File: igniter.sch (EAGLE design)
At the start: 19 parts, among them X1 RASPI_BOARD_B+#_H, X3 5566-4-RIGHTANGLE

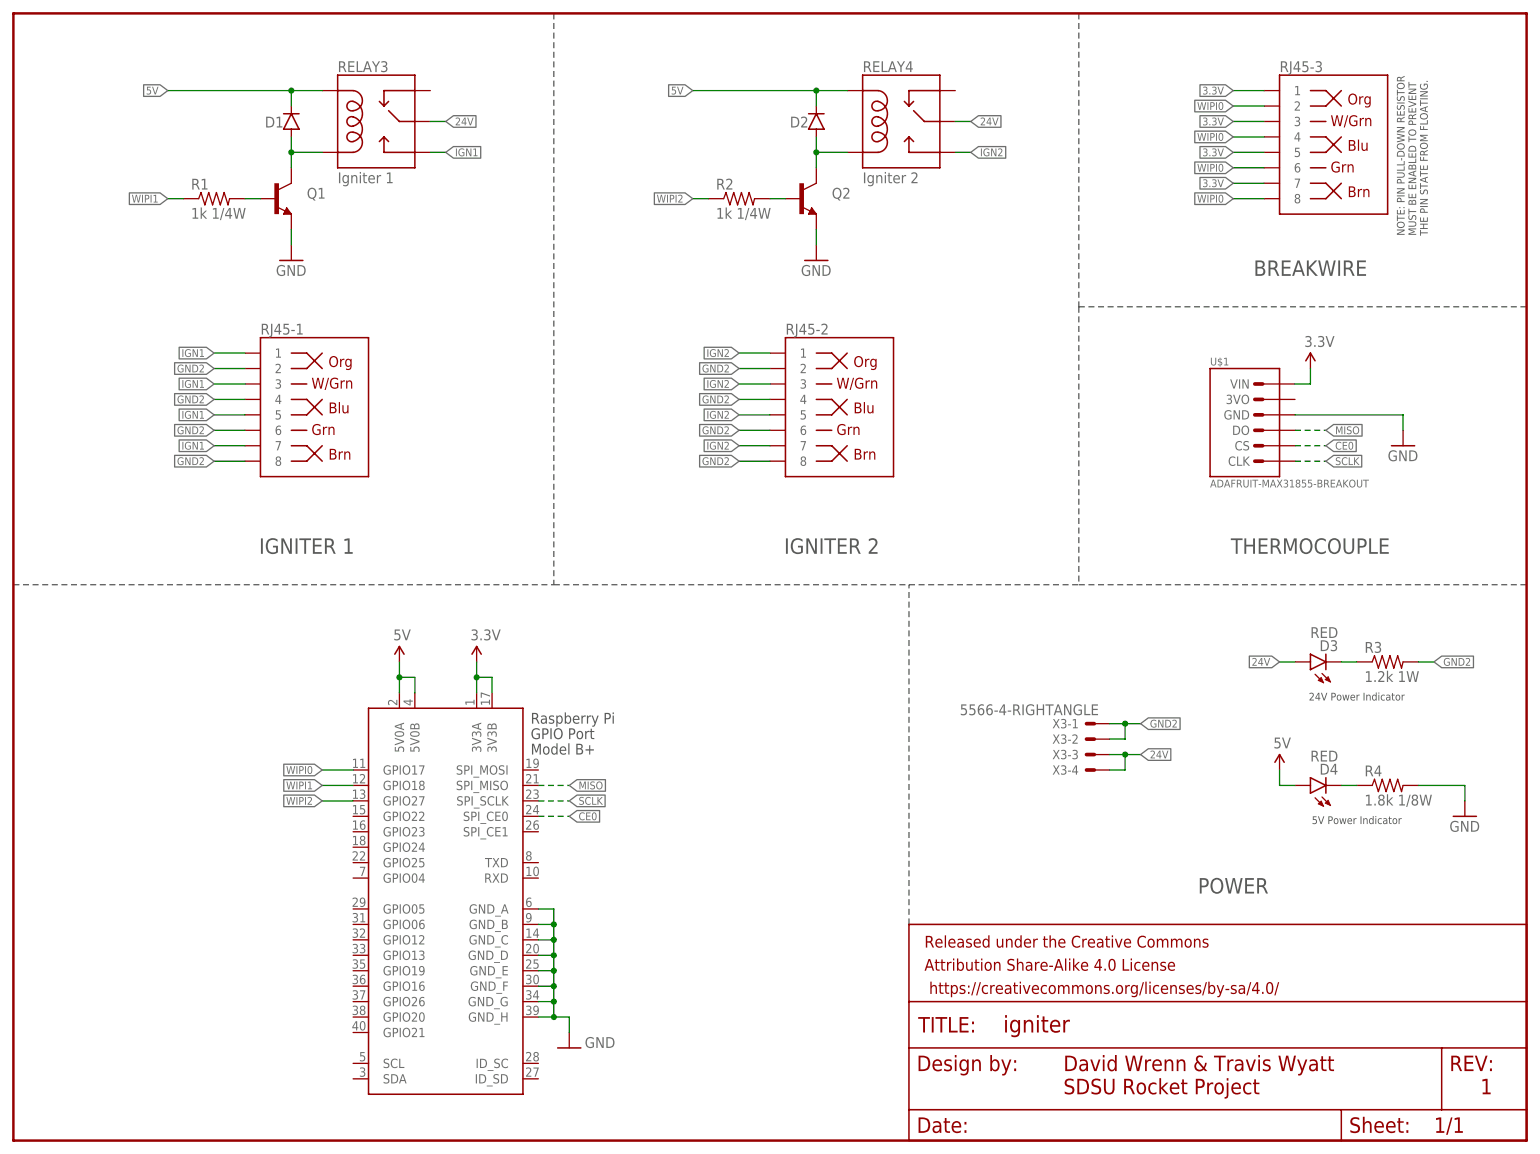
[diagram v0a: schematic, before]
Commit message: Power connector and resistor updates. Added PCB images (generated by OSHPark). Added README.md.
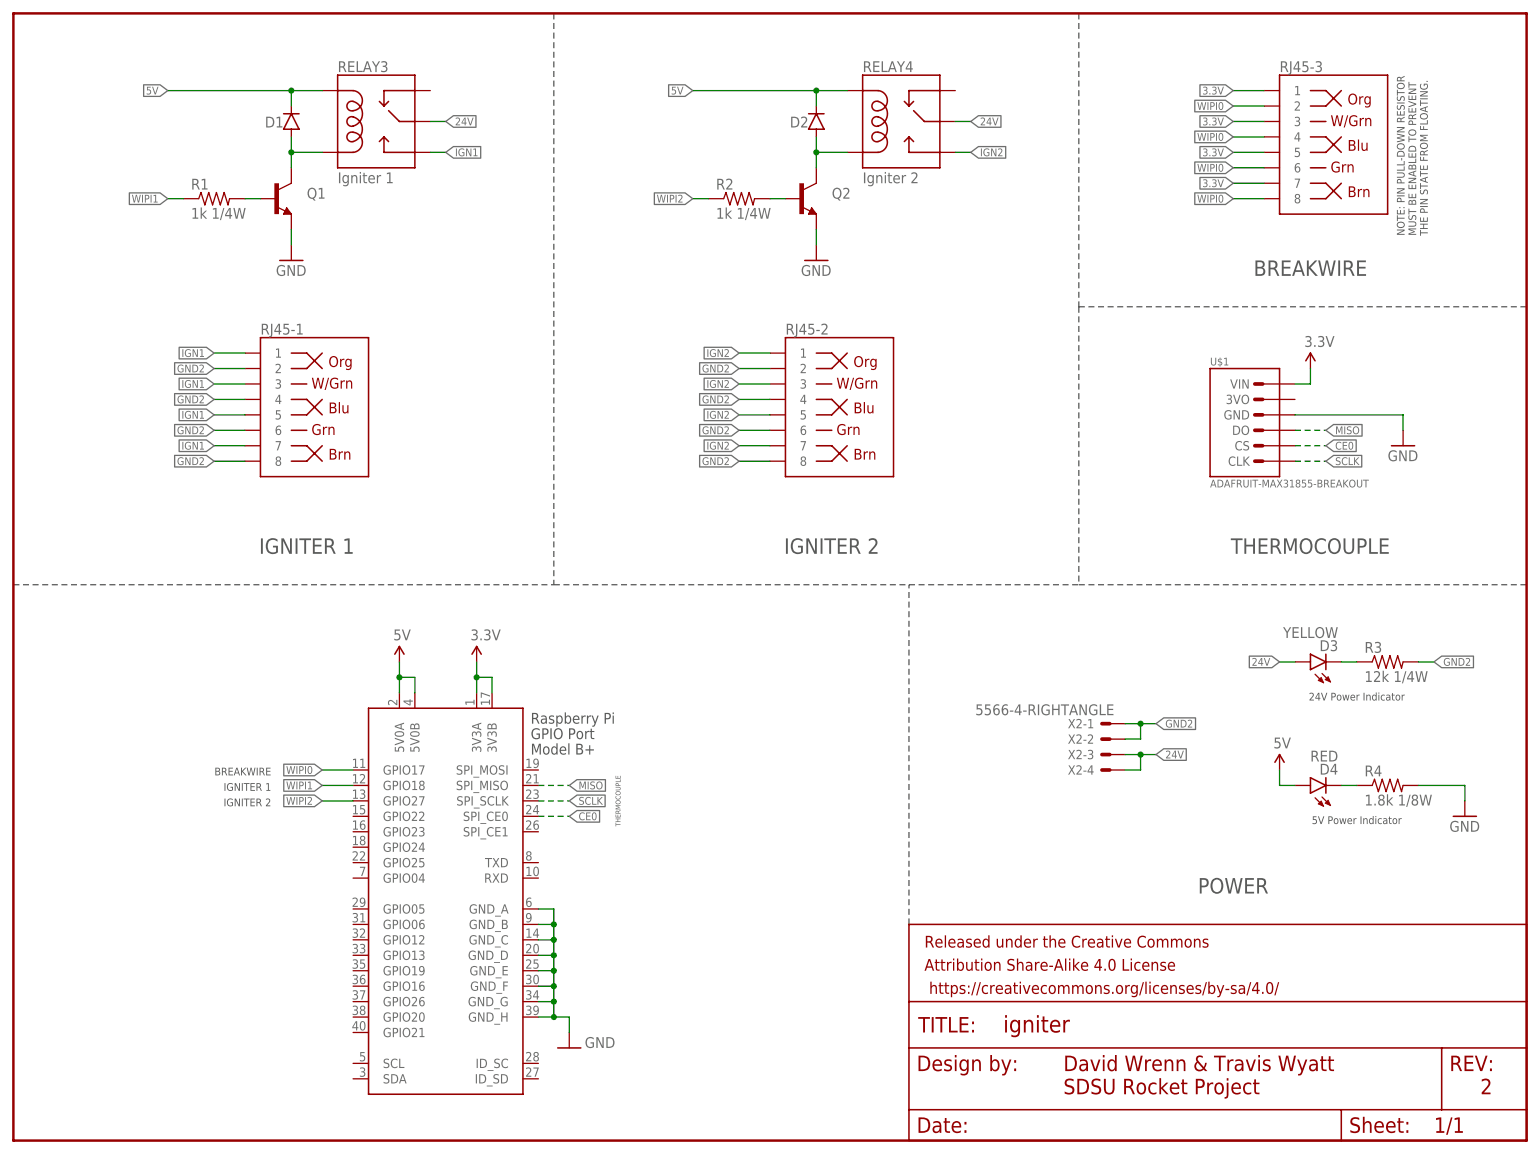
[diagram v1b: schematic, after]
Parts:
- removed X3: 5566-4-RIGHTANGLE, SDSURocket-BreakoutBoards:5566-4-RIGHTANGLE
- added X2: 5566-4-RIGHTANGLE, SDSURocket-Connectors:5566-4-RIGHTANGLE
- D3: value RED -> YELLOW
- R3: value 1.2k 1W -> 12k 1/4W; device SparkFun-Resistors:RESISTOR2512 -> SparkFun-Resistors:RESISTOR0603-RES
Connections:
- net 24V: now also X2-3.S, X2-4.S; no longer X3-3.S, X3-4.S
- net GND2: now also X2-1.S, X2-2.S; no longer X3-1.S, X3-2.S
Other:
- note added: "2"
- note removed: "1"
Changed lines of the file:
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@@
 <part name="RJ45-3" library="SparkFun-Connectors" deviceset="RJ45-8" device="PTH" value=""/>
 <part name="U$1" library="SDSURocket-BreakoutBoards" deviceset="ADAFRUIT-MAX31855" device="-BREAKOUT"/>
-<part name="X3" library="SDSURocket-BreakoutBoards" deviceset="5566-4" device="-RIGHTANGLE"/>
-<part name="D3" library="SparkFun-LED" deviceset="LED" device="0603" value="RED"/>
+<part name="D3" library="SparkFun-LED" deviceset="LED" device="0603" value="YELLOW"/>
 <part name="D4" library="SparkFun-LED" deviceset="LED" device="0603" value="RED"/>
-<part name="R3" library="SparkFun-Resistors" deviceset="RESISTOR" device="2512" value="1.2k 1W"/>
+<part name="R3" library="SparkFun-Resistors" deviceset="RESISTOR" device="0603-RES" value="12k 1/4W"/>
 <part name="R4" library="SparkFun-Resistors" deviceset="RESISTOR" device="0603-RES" value="1.8k 1/8W"/>
 <part name="GND2" library="SparkFun-Aesthetics" deviceset="GND" device=""/>
@@
 <part name="SUPPLY3" library="SparkFun-Aesthetics" deviceset="3.3V" device=""/>
 <part name="SUPPLY4" library="SparkFun-Aesthetics" deviceset="5V" device=""/>
+<part name="X2" library="SDSURocket-Connectors" deviceset="5566-4" device="-RIGHTANGLE"/>
 </parts>
 <sheets>
@@
 MUST BE ENABLED TO PREVENT
 THE PIN STATE FROM FLOATING.</text>
-<text x="241.3" y="7.62" size="2.54" layer="94">1</text>
+<text x="241.3" y="7.62" size="2.54" layer="94">2</text>
 <text x="172.72" y="12.7" size="2.54" layer="94" align="center-left">David Wrenn &amp; Travis Wyatt</text>
 <text x="172.72" y="8.89" size="2.54" layer="94" align="center-left">SDSU Rocket Project</text>
 <text x="220.98" y="73.66" size="1.27" layer="97" align="top-center">24V Power Indicator</text>
 <text x="220.98" y="53.34" size="1.27" layer="97" align="top-center">5V Power Indicator</text>
+<text x="42.418" y="60.706" size="1.27" layer="97" align="center-right">BREAKWIRE</text>
+<text x="42.418" y="58.166" size="1.27" layer="97" align="center-right">IGNITER 1</text>
+<text x="42.418" y="55.626" size="1.27" layer="97" align="center-right">IGNITER 2</text>
+<text x="99.06" y="55.88" size="0.8128" layer="97" rot="R90" align="top-center">THERMOCOUPLE</text>
 </plain>
 <instances>
@@
 <instance part="RJ45-3" gate="JP1" x="213.36" y="165.1"/>
 <instance part="U$1" gate="G$1" x="203.2" y="119.38"/>
-<instance part="X3" gate="-1" x="177.8" y="68.58" rot="MR0"/>
-<instance part="X3" gate="-2" x="177.8" y="66.04" rot="MR0"/>
-<instance part="X3" gate="-3" x="177.8" y="63.5" rot="MR0"/>
-<instance part="X3" gate="-4" x="177.8" y="60.96" rot="MR0"/>
 <instance part="D3" gate="G$1" x="213.36" y="78.74" rot="R90"/>
 <instance part="D4" gate="G$1" x="213.36" y="58.42" rot="R90"/>
@@
 <instance part="SUPPLY3" gate="G$1" x="213.36" y="127"/>
 <instance part="SUPPLY4" gate="G$1" x="208.28" y="60.96"/>
+<instance part="X2" gate="-1" x="180.34" y="68.58" rot="MR0"/>
+<instance part="X2" gate="-2" x="180.34" y="66.04" rot="MR0"/>
+<instance part="X2" gate="-3" x="180.34" y="63.5" rot="MR0"/>
+<instance part="X2" gate="-4" x="180.34" y="60.96" rot="MR0"/>
 </instances>
 <busses>
@@
 </segment>
 <segment>
-<pinref part="X3" gate="-3" pin="S"/>
-<wire x1="180.34" y1="63.5" x2="182.88" y2="63.5" width="0.1524" layer="91"/>
-<pinref part="X3" gate="-4" pin="S"/>
-<wire x1="182.88" y1="63.5" x2="185.42" y2="63.5" width="0.1524" layer="91"/>
-<wire x1="180.34" y1="60.96" x2="182.88" y2="60.96" width="0.1524" layer="91"/>
-<wire x1="182.88" y1="60.96" x2="182.88" y2="63.5" width="0.1524" layer="91"/>
-<junction x="182.88" y="63.5"/>
-<label x="185.42" y="63.5" size="1.27" layer="95" xref="yes"/>
-</segment>
-<segment>
 <pinref part="D3" gate="G$1" pin="A"/>
 <wire x1="210.82" y1="78.74" x2="208.28" y2="78.74" width="0.1524" layer="91"/>
 <label x="208.28" y="78.74" size="1.27" layer="95" rot="MR0" xref="yes"/>
+</segment>
+<segment>
+<pinref part="X2" gate="-3" pin="S"/>
+<wire x1="182.88" y1="63.5" x2="185.42" y2="63.5" width="0.1524" layer="91"/>
+<pinref part="X2" gate="-4" pin="S"/>
+<wire x1="185.42" y1="63.5" x2="187.96" y2="63.5" width="0.1524" layer="91"/>
+<wire x1="182.88" y1="60.96" x2="185.42" y2="60.96" width="0.1524" layer="91"/>
+<wire x1="185.42" y1="60.96" x2="185.42" y2="63.5" width="0.1524" layer="91"/>
+<junction x="185.42" y="63.5"/>
+<label x="187.96" y="63.5" size="1.27" layer="95" xref="yes"/>
 </segment>
 </net>
@@
 </segment>
 <segment>
-<pinref part="X3" gate="-1" pin="S"/>
-<wire x1="180.34" y1="68.58" x2="182.88" y2="68.58" width="0.1524" layer="91"/>
-<pinref part="X3" gate="-2" pin="S"/>
-<wire x1="182.88" y1="68.58" x2="185.42" y2="68.58" width="0.1524" layer="91"/>
-<wire x1="180.34" y1="66.04" x2="182.88" y2="66.04" width="0.1524" layer="91"/>
-<wire x1="182.88" y1="66.04" x2="182.88" y2="68.58" width="0.1524" layer="91"/>
-<junction x="182.88" y="68.58"/>
-<label x="185.42" y="68.58" size="1.27" layer="95" xref="yes"/>
-</segment>
-<segment>
 <pinref part="R3" gate="G$1" pin="2"/>
 <wire x1="231.14" y1="78.74" x2="233.68" y2="78.74" width="0.1524" layer="91"/>
 <label x="233.68" y="78.74" size="1.27" layer="95" xref="yes"/>
 </segment>
-</net>
+<segment>
+<pinref part="X2" gate="-1" pin="S"/>
+<wire x1="182.88" y1="68.58" x2="185.42" y2="68.58" width="0.1524" layer="91"/>
+<pinref part="X2" gate="-2" pin="S"/>
+<wire x1="185.42" y1="68.58" x2="187.96" y2="68.58" width="0.1524" layer="91"/>
+<wire x1="182.88" y1="66.04" x2="185.42" y2="66.04" width="0.1524" layer="91"/>
+<wire x1="185.42" y1="66.04" x2="185.42" y2="68.58" width="0.1524" layer="91"/>
+<junction x="185.42" y="68.58"/>
+<label x="187.96" y="68.58" size="1.27" layer="95" xref="yes"/>
+</segment>
+</net>
